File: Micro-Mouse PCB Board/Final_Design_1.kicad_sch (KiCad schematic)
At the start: 11 parts, among them J3 Conn_02x16_Odd_Even, Q5 PMOS, Q6 Q_NMOS, U8 BQ24091DGQR, U9 INA219AxD

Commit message: Latest Files
v1.0.1 Micro-Mouse PCB Files
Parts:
- removed Q6: Q_NMOS, symbol Device:Q_NMOS
- removed S2: EG1213, EG1213:SW_EG1213, symbol EG1213:EG1213
- removed U8: BQ24091DGQR, BQ24091DGQR:IC_XTR111AIDGQR, symbol BQ24091DGQR:BQ24091DGQR
- added Q2: NMOS, symbol Simulation_SPICE:NMOS
- added S1: EG1213, Micro-Mouse Component Footprints:SW_EG1213, symbol Micro-Mouse Symbol Library:EG1213
- added U1: ~, symbol Device:LiPo_Battery
- added U2: BQ24091DGQR, Micro-Mouse Component Footprints:BQ24091DGQR, symbol Micro-Mouse Symbol Library:BQ24091DGQR
- U3: renamed from U9; Price $3.75 -> $5.98
- renumbered C8 to C1, C9 to C2, J3 to J1, Q5 to Q1, R12 to R1, R13 to R2, R14 to R3
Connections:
- net 9V USB-C Input: now also U2.1 (IN)
- net FAST_CHARGE_CTRL: now also Q2.2 (G)
- net GND: now also Q2.1 (D), S1.1, U1.2 (-), U2.3 (VSS)
- net ISET2: now also Q2.3 (S), U2.7 (ISET2); no longer R1.2, R2.1
- net Positive Battery Terminal: now also S1.2, U1.1 (+), U2.10 (OUT)
- net Voltage Regulator Input: now also S1.3
- new net: R2.1, U2.4 (PRETERM)
- new net: R1.2, U2.2 (ISET)
- no-connect marks 3 -> 4
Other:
- note added: "Negative Battery Terminal"
- note removed: "GND"

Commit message: v1.0.2
A few changes to the battery charger
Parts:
- added D1, D2: LED, symbol Device:LED
- added Q3: NMOS, symbol Simulation_SPICE:NMOS
- added R4, R5: 1.5k, symbol Device:R_US
- added R6: 1.35k, symbol Device:R_US
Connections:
- net 9V USB-C Input: no longer Q1.3 (S)
- net FAST_CHARGE_CTRL: now also Q3.2 (G)
- net GND: now also U2.7 (ISET2), Q3.3 (S)
- net Positive Battery Terminal: now also R4.2, R5.2
- net at R1.2, U2.2 (ISET): now also R6.1
- net at U2.5 (~{PG}): now also D2.1 (K)
- net at U2.8 (~{CHG}): now also D1.1 (K)
- net ISET2: no longer names the net of Q1.1 (D), Q2.3 (S)
- net ISET2: no longer U2.7 (ISET2)
- new net: Q3.1 (D), R6.2
- new net: D1.2 (A), R4.1
- new net: D2.2 (A), R5.1
- no-connect marks 4 -> 2
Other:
- note added: "ISET2"
- moved on the sheet: Q1, Q2, R1

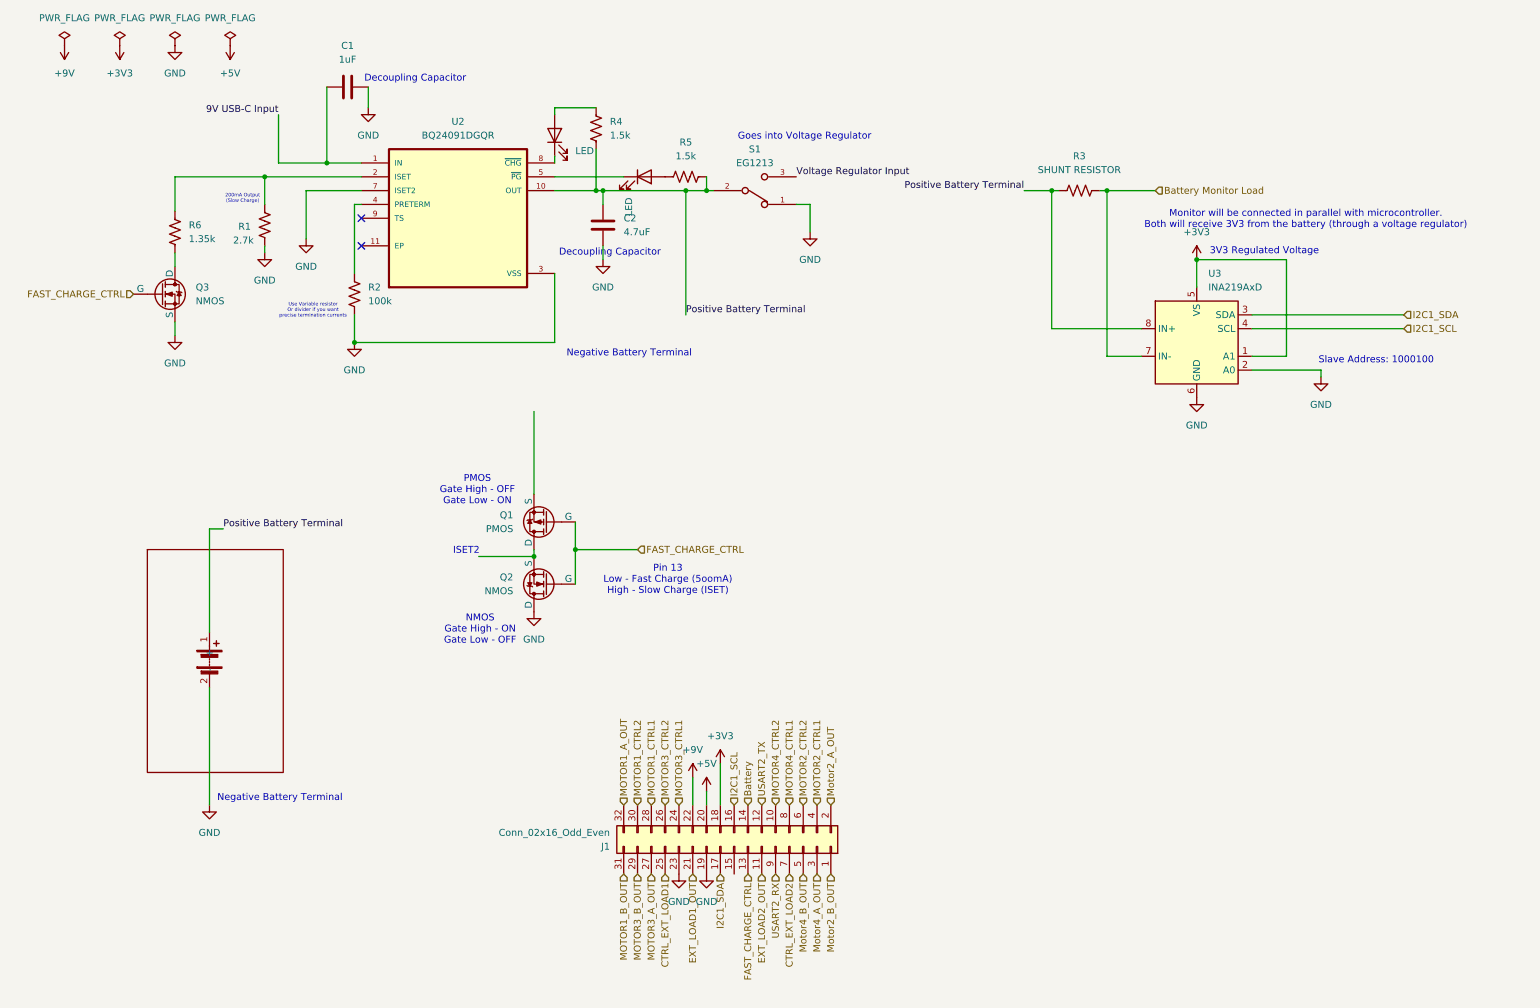
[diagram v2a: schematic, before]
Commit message: Footprints and Symbols
Uploaded components footprints and symbols
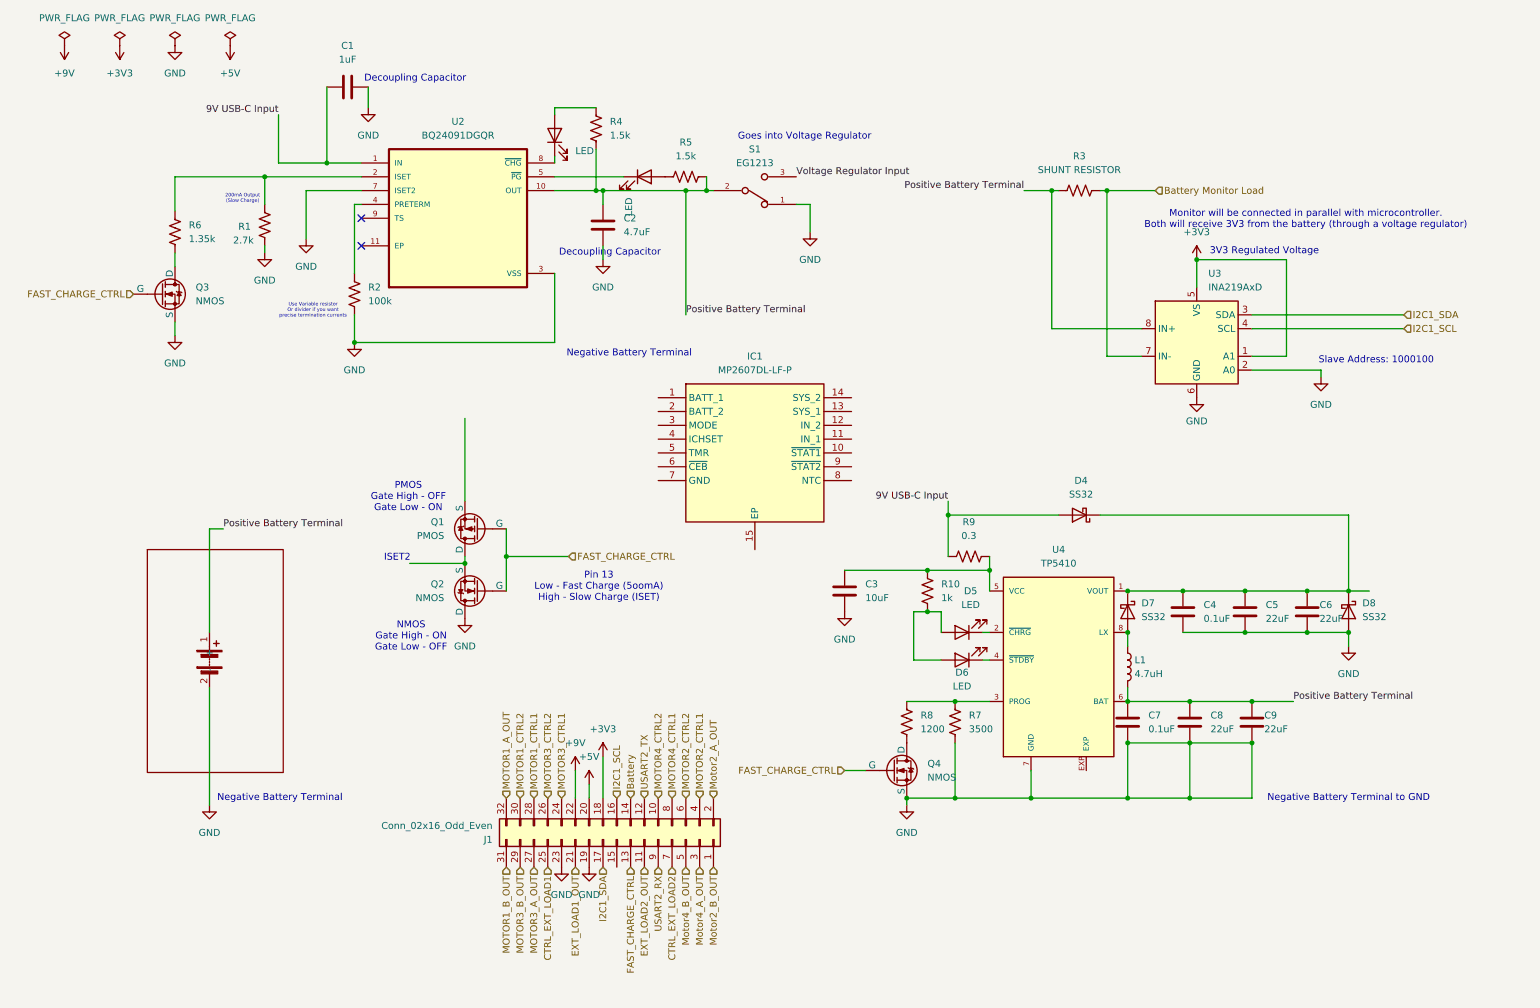
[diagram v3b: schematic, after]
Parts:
- added C3: 10uF, symbol Device:C
- added C4, C7: 0.1uF, symbol Device:C
- added C5, C6, C8, C9: 22uF, symbol Device:C
- added D4, D7, D8: SS32, Diode_SMD:D_SMA, symbol Diode:SS32
- added D5, D6: LED, symbol Device:LED
- added IC1: MP2607DL-LF-P, SON50P300X400X100-15N-D, symbol MP2607DL-LF-P:MP2607DL-LF-P
- added L1: 4.7uH, symbol Device:L
- added Q4: NMOS, symbol Simulation_SPICE:NMOS
- added R10: 1k, symbol Device:R_US
- added R7: 3500, symbol Device:R_US
- added R8: 1200, symbol Device:R_US
- added R9: 0.3, symbol Device:R_US
- added U4: TP5410, TP5410:SOP8-P, symbol TP5410:TP5410
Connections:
- net 9V USB-C Input: now also D4.2 (A), R9.1
- net FAST_CHARGE_CTRL: now also Q4.2 (G)
- net GND: now also C3.2, C4.2, C5.2, C6.2, C7.2, C8.2, C9.2, D8.2 (A), Q4.3 (S), R7.2, U4.7 (GND)
- net Positive Battery Terminal: now also C7.1, C8.1, C9.1, L1.2, U4.6 (BAT)
- new net: Q4.1 (D), R8.2
- new net: C3.1, R10.2, R9.2, U4.5 (VCC)
- new net: D5.2 (A), D6.2 (A), R10.1
- new net: R7.1, R8.1, U4.3 (PROG)
- new net: C4.1, C5.1, C6.1, D4.1 (K), D7.1 (K), D8.1 (K), U4.1 (VOUT)
- new net: D7.2 (A), L1.1, U4.8 (LX)
- new net: D5.1 (K), U4.2 (~{CHRG})
- new net: D6.1 (K), U4.4 (~{STDBY})
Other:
- note added: "Negative Battery Terminal to GND"
- moved on the sheet: J1, Q1, Q2
